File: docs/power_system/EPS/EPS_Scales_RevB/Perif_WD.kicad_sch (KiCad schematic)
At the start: 40 parts, among them J2 Breakout, J3 Breakout, U1 TLV1704

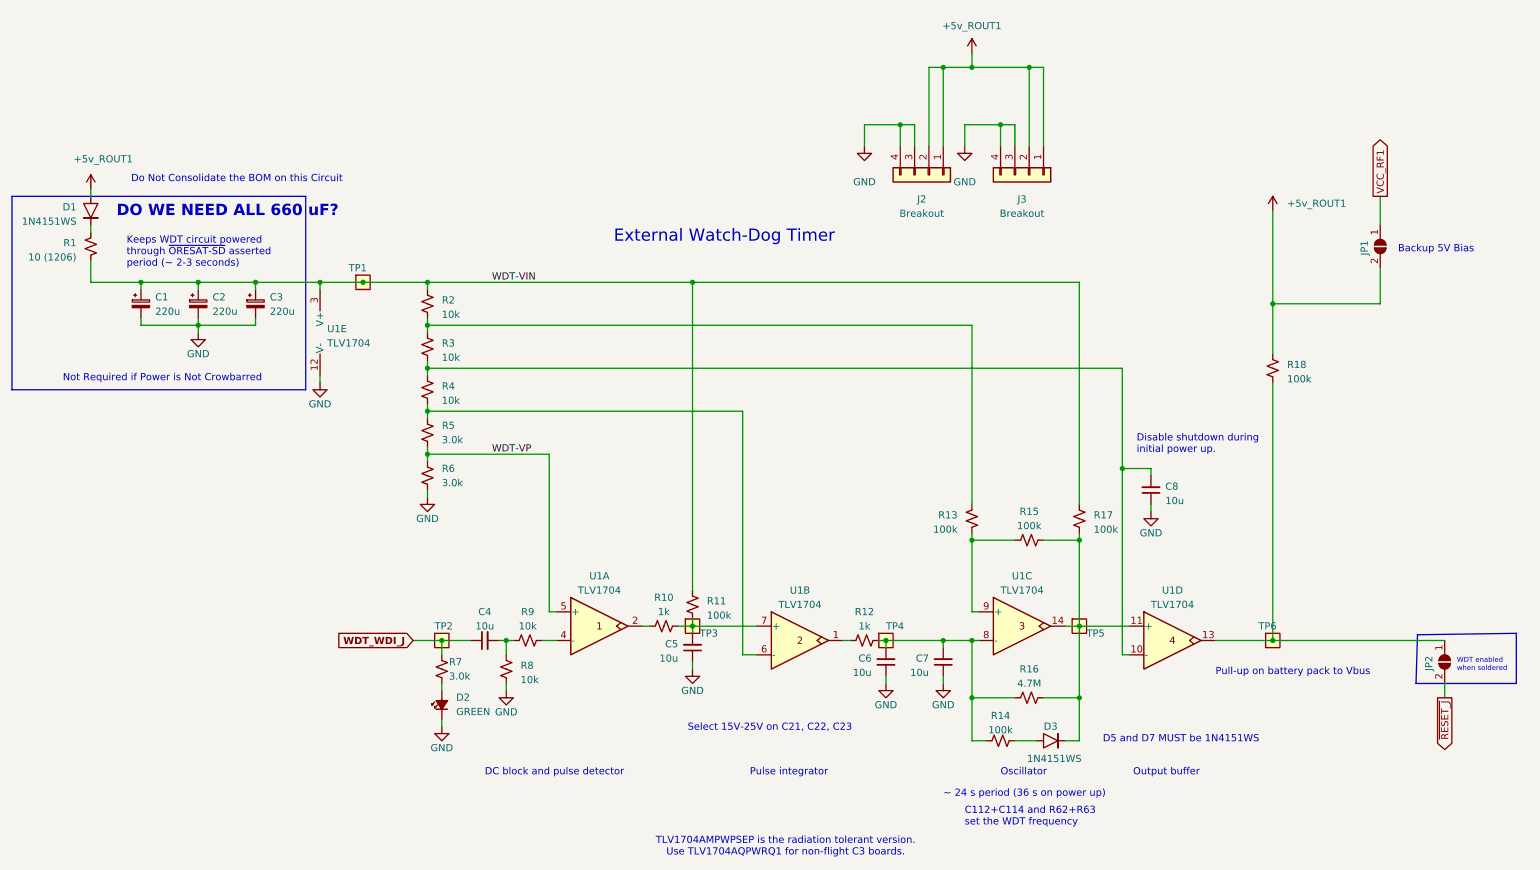
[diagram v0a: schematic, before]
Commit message: Rev_B_EPS Schematic Updates
EPS Board Schematic is starting to come to a conclusion. Swapped out to new load switches that use external mosfets and have an enable switch. R and C values finalized for almost everything. Need some reviewing and/or notes on how to proceed with Phases for each component plus if we might need an external DC/DC converter just for the clock oscillator. Good stuff
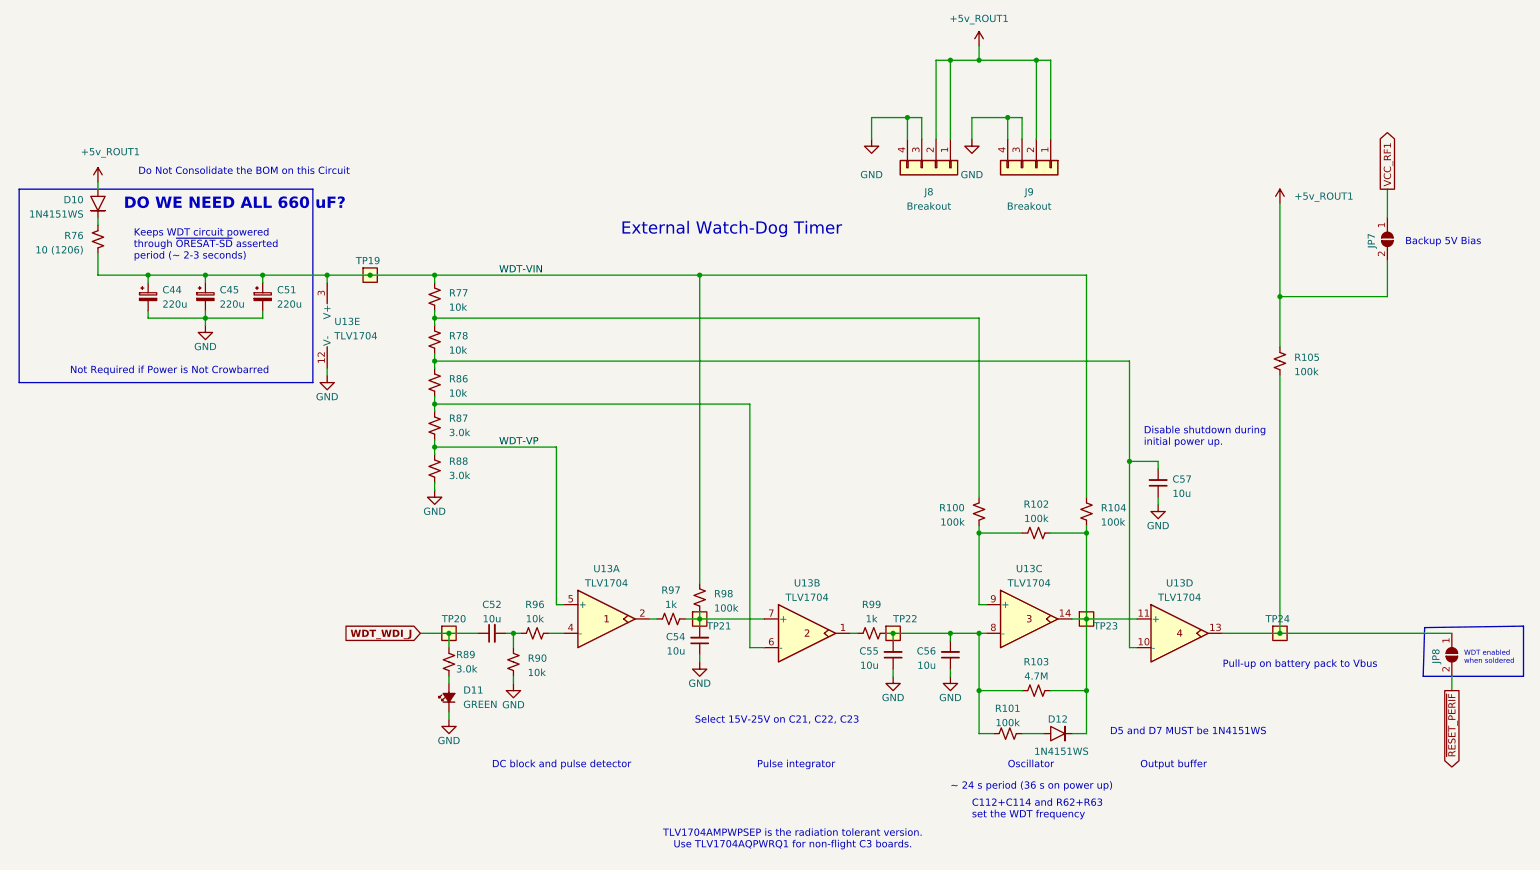
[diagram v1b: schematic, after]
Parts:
- removed C1, C2, C3: 220u, Capacitor_Tantalum_SMD:CP_EIA-7361-38_AVX-V, symbol Device:C_Polarized_Small
- removed C4, C5, C6, C7, C8: 10u, Capacitor_SMD:C_0603_1608Metric, symbol Device:C_Small
- removed D1, D3: 1N4151WS, Diode_SMD:D_SOD-323, symbol oresat-diodes:1N4151WS-HE3
- removed D2: GREEN, LED_SMD:LED_0603_1608Metric, symbol Device:LED_Small_Filled
- removed J2: Breakout, Connector_PinHeader_2.54mm:PinHeader_1x04_P2.54mm_Vertical, symbol Connector_Generic:Conn_01x04
- removed J3: Breakout, FC_DEV_BOARD:JST_BM04B-SRSS-TB(LF)(SN), symbol Connector_Generic:Conn_01x04
- removed JP1, JP2: SolderJumper_2_Open, Jumper:SolderJumper-2_P1.3mm_Open_RoundedPad1.0x1.5mm, symbol Jumper:SolderJumper_2_Open
- removed R1: 10 (1206), Resistor_SMD:R_1206_3216Metric, symbol Device:R_Small_US
- removed R10, R12: 1k, Resistor_SMD:R_0603_1608Metric, symbol Device:R_Small_US
- removed R11, R13, R14, R15, R17, R18: 100k, Resistor_SMD:R_0603_1608Metric, symbol Device:R_Small_US
- removed R16: 4.7M, Resistor_SMD:R_0603_1608Metric, symbol Device:R_Small_US
- removed R2, R3, R4, R8, R9: 10k, Resistor_SMD:R_0603_1608Metric, symbol Device:R_Small_US
- removed R5, R6, R7: 3.0k, Resistor_SMD:R_0603_1608Metric, symbol Device:R_Small_US
- removed TP1, TP2, TP3, TP4, TP5, TP6: TestPoint-MinTH, oresat-misc:TestPoint-0.75mm-th, symbol oresat-misc:Test-Point-0.75mm-th
- removed U1: TLV1704, Package_SO:TSSOP-14_4.4x5mm_P0.65mm, symbol oresat-ics:TLV1704AIPWR
- added C44, C45, C51: 220u, Capacitor_Tantalum_SMD:CP_EIA-7361-38_AVX-V, symbol Device:C_Polarized_Small
- added C52, C54, C55, C56, C57: 10u, Capacitor_SMD:C_0603_1608Metric, symbol Device:C_Small
- added D10, D12: 1N4151WS, Diode_SMD:D_SOD-323, symbol oresat-diodes:1N4151WS-HE3
- added D11: GREEN, LED_SMD:LED_0603_1608Metric, symbol Device:LED_Small_Filled
- added J8: Breakout, Connector_PinHeader_2.54mm:PinHeader_1x04_P2.54mm_Vertical, symbol Connector_Generic:Conn_01x04
- added J9: Breakout, FC_DEV_BOARD:JST_BM04B-SRSS-TB(LF)(SN), symbol Connector_Generic:Conn_01x04
- added JP7, JP8: SolderJumper_2_Open, Jumper:SolderJumper-2_P1.3mm_Open_RoundedPad1.0x1.5mm, symbol Jumper:SolderJumper_2_Open
- added R100, R101, R102, R104, R105, R98: 100k, Resistor_SMD:R_0603_1608Metric, symbol Device:R_Small_US
- added R103: 4.7M, Resistor_SMD:R_0603_1608Metric, symbol Device:R_Small_US
- added R76: 10 (1206), Resistor_SMD:R_1206_3216Metric, symbol Device:R_Small_US
- added R77, R78, R86, R90, R96: 10k, Resistor_SMD:R_0603_1608Metric, symbol Device:R_Small_US
- added R87, R88, R89: 3.0k, Resistor_SMD:R_0603_1608Metric, symbol Device:R_Small_US
- added R97, R99: 1k, Resistor_SMD:R_0603_1608Metric, symbol Device:R_Small_US
- added TP19, TP20, TP21, TP22, TP23, TP24: TestPoint-MinTH, oresat-misc:TestPoint-0.75mm-th, symbol oresat-misc:Test-Point-0.75mm-th
- added U13: TLV1704, Package_SO:TSSOP-14_4.4x5mm_P0.65mm, symbol oresat-ics:TLV1704AIPWR
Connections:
- net +5v_ROUT1: now also D10.2, J8.1 (Pin_1), J8.2 (Pin_2), J9.1 (Pin_1), J9.2 (Pin_2), JP7.2 (B), R105.2
- net GND: now also C44.2, C45.2, C51.2, C54.1, C55.1, C56.1, C57.1, D11.1 (K), J8.3 (Pin_3), J8.4 (Pin_4), J9.3 (Pin_3), J9.4 (Pin_4), R88.2, R90.2, U13.12 (V-)
- net VCC_RF1: now also JP7.1 (A)
- net WDT-VIN: now also C44.1, C45.1, C51.1, R104.2, R76.2, R77.1, R98.1, TP19.1, U13.3 (V+)
- net WDT-VP: now also R87.2, R88.1, U13.5 (+)
- net WDT_WDI_J: now also C52.1, R89.1, TP20.1
- new net: R100.2, R77.2, R78.1
- new net: C57.2, R78.2, R86.1, U13.10 (-)
- new net: D10.1, R76.1
- new net: D12.1, R102.2, R103.1, R104.1, TP23.1, U13.11 (+), U13.14
- new net: C55.2, C56.2, R101.2, R103.2, R99.2, TP22.1, U13.8 (-)
- new net: R100.1, R102.1, U13.9 (+)
- new net: R86.2, R87.1, U13.6 (-)
- new net: C52.2, R90.1, R96.1
- new net: C54.2, R97.2, R98.2, TP21.1, U13.7 (+)
- new net: R97.1, U13.2
- new net: JP8.1 (A), R105.1, TP24.1, U13.13
- new net: D12.2, R101.1
- new net: R96.2, U13.4 (-)
- new net: R99.1, U13.1
- new net: D11.2 (A), R89.2
- new net ~{RESET_PERIF}: JP8.2 (B)
